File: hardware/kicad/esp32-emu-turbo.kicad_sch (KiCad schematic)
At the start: 53 parts, among them J1 USB_C, J2 PSP_Joystick, SW1 UP, SW10 SELECT, SW11 L, SW12 R, SW2 DOWN, SW3 LEFT, SW4 RIGHT, SW5 A, SW6 B, SW7 X, SW8 Y, SW9 START, U1 ESP32-S3-N16R8, U2 IP5306_USB-C, U3 AMS1117-3.3, U4 ST7796S 4.0in 8080, U5 PAM8403, U6 SD_Card_SPI

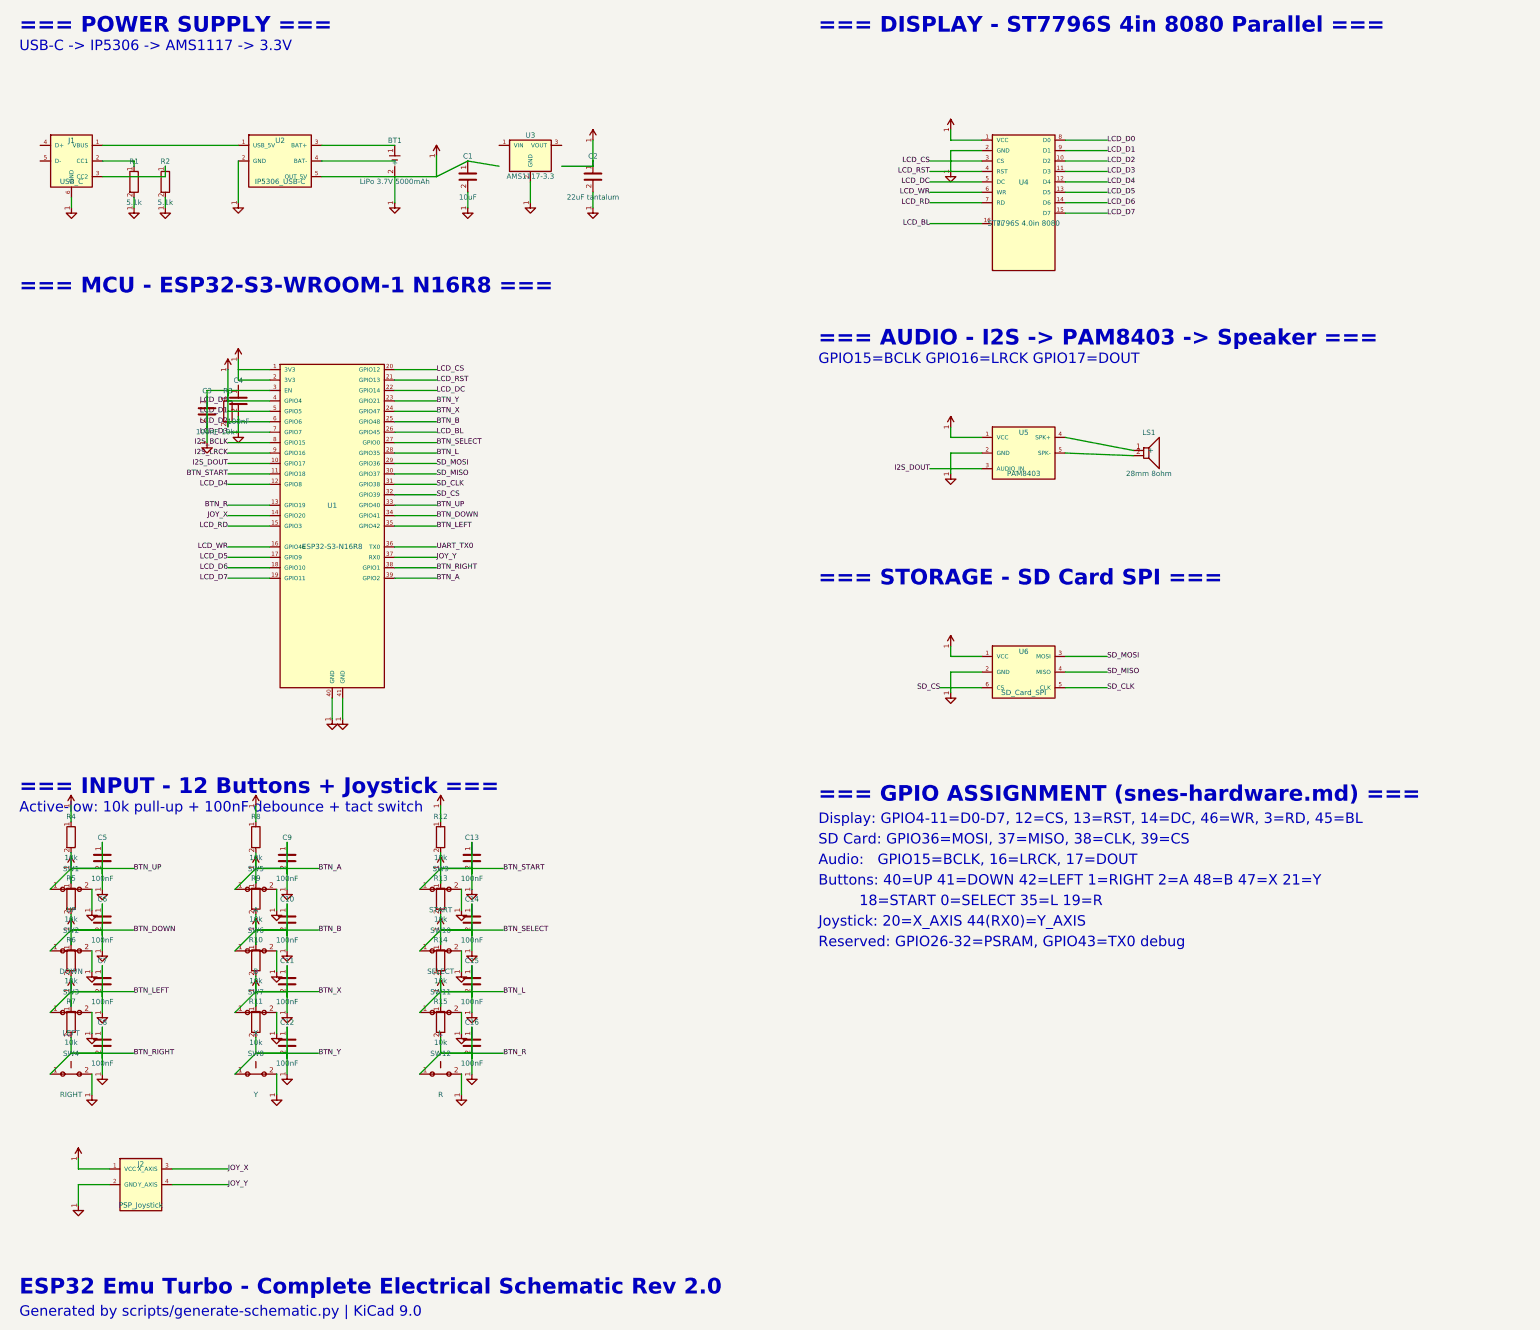
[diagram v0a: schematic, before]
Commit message: Add PCB layout, hierarchical schematics, verification & rendering pipeline
- Reorganize passive components into centered rows below ESP32
- Add missing schematic symbols (LED, FPC_16P, SW_PWR, SW13, SPK1)
- Generate hierarchical root schematic with 7 sub-sheet references
- Create PCB layout generator (4-layer, 160x75mm, JLCPCB-ready)
- Add JLCPCB export (BOM.csv + CPL.csv for 65 components)
- Add schematic/PCB/JLCPCB consistency verification script
- Add PCB SVG renderer + PNG/GIF animation pipeline
- Add interactive 3D PCB viewer (Three.js)
- Update docs (pcb.md, components.md, README.md)

Co-Authored-By: Claude Opus 4.6 <noreply@anthropic.com>
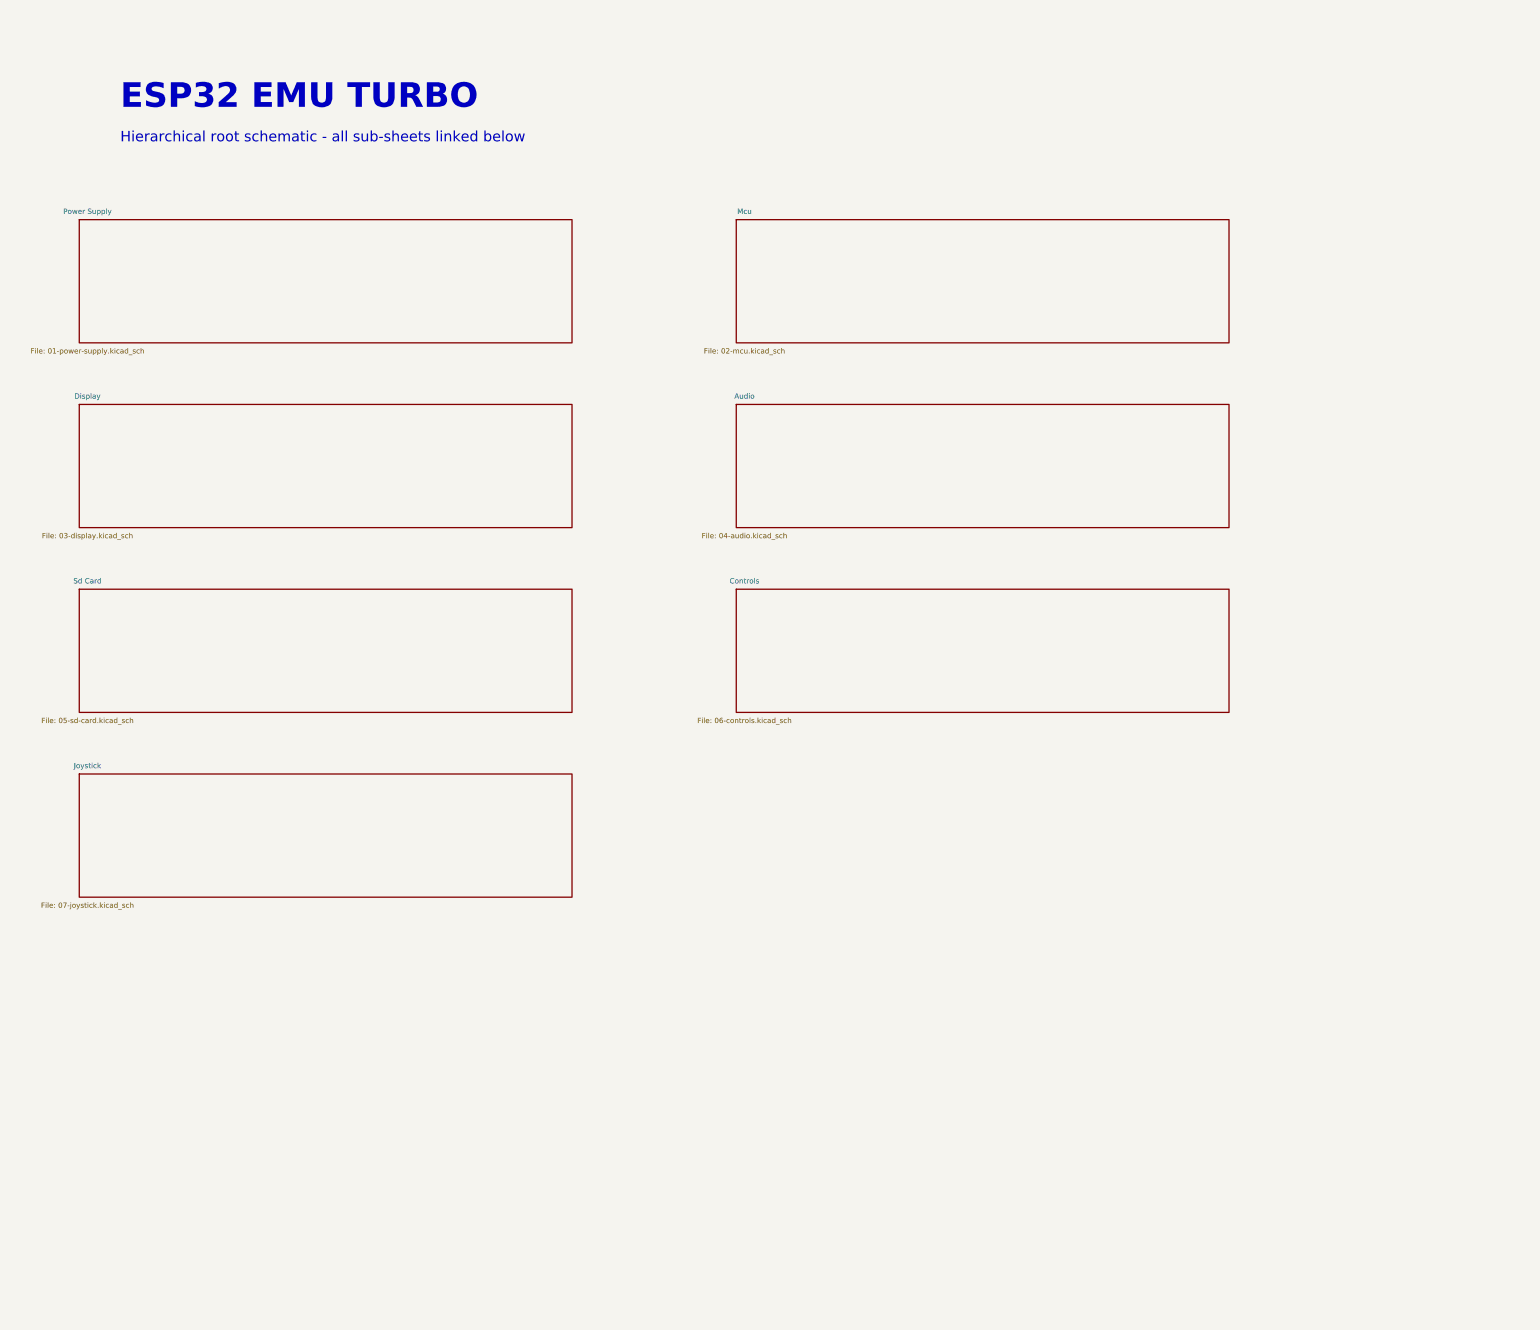
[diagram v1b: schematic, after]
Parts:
- removed BT1: LiPo 3.7V 5000mAh, symbol Battery
- removed C1: 10uF, symbol C
- removed C10, C11, C12, C13, C14, C15, C16, C3, C4, C5, C6, C7, C8, C9: 100nF, symbol C
- removed C2: 22uF tantalum, symbol C
- removed J1: USB_C, symbol USB_C
- removed J2: PSP_Joystick, symbol PSP_Joystick
- removed LS1: 28mm 8ohm, symbol Speaker
- removed R1, R2: 5.1k, symbol R
- removed R10, R11, R12, R13, R14, R15, R3, R4, R5, R6, R7, R8, R9: 10k, symbol R
- removed SW1: UP, symbol SW_Push
- removed SW10: SELECT, symbol SW_Push
- removed SW11: L, symbol SW_Push
- removed SW12: R, symbol SW_Push
- removed SW2: DOWN, symbol SW_Push
- removed SW3: LEFT, symbol SW_Push
- removed SW4: RIGHT, symbol SW_Push
- removed SW5: A, symbol SW_Push
- removed SW6: B, symbol SW_Push
- removed SW7: X, symbol SW_Push
- removed SW8: Y, symbol SW_Push
- removed SW9: START, symbol SW_Push
- removed U1: ESP32-S3-N16R8, symbol ESP32-S3-WROOM-1
- removed U2: IP5306_USB-C, symbol IP5306_Module
- removed U3: AMS1117-3.3, symbol AMS1117-3.3
- removed U4: ST7796S 4.0in 8080, symbol ST7796S_Module
- removed U5: PAM8403, symbol PAM8403_Module
- removed U6: SD_Card_SPI, symbol SD_Module
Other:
- added sheet Audio (04-audio.kicad_sch)
- added sheet Controls (06-controls.kicad_sch)
- added sheet Display (03-display.kicad_sch)
- added sheet Joystick (07-joystick.kicad_sch)
- added sheet Mcu (02-mcu.kicad_sch)
- added sheet Power Supply (01-power-supply.kicad_sch)
- added sheet Sd Card (05-sd-card.kicad_sch)
- note added: "ESP32 EMU TURBO"
- note added: "Hierarchical root schematic - all sub-sheets linked below"
- note removed: "18=START 0=SELECT 35=L 19=R"
- note removed: "=== AUDIO - I2S -> PAM8403 -> Speaker ==="
- note removed: "=== DISPLAY - ST7796S 4in 8080 Parallel ==="
- note removed: "=== GPIO ASSIGNMENT (snes-hardware.md) ==="
- note removed: "=== INPUT - 12 Buttons + Joystick ==="
- note removed: "=== MCU - ESP32-S3-WROOM-1 N16R8 ==="
- note removed: "=== POWER SUPPLY ==="
- note removed: "=== STORAGE - SD Card SPI ==="
- note removed: "Active-low: 10k pull-up + 100nF debounce + tact switch"
- note removed: "Audio: GPIO15=BCLK, 16=LRCK, 17=DOUT"
- note removed: "Buttons: 40=UP 41=DOWN 42=LEFT 1=RIGHT 2=A 48=B 47=X 21=Y"
- note removed: "Display: GPIO4-11=D0-D7, 12=CS, 13=RST, 14=DC, 46=WR, 3=RD, 45=BL"
- note removed: "ESP32 Emu Turbo - Complete Electrical Schematic Rev 2.0"
- note removed: "GPIO15=BCLK GPIO16=LRCK GPIO17=DOUT"
- note removed: "Generated by scripts/generate-schematic.py | KiCad 9.0"
- note removed: "Joystick: 20=X_AXIS 44(RX0)=Y_AXIS"
- note removed: "Reserved: GPIO26-32=PSRAM, GPIO43=TX0 debug"
- note removed: "SD Card: GPIO36=MOSI, 37=MISO, 38=CLK, 39=CS"
- note removed: "USB-C -> IP5306 -> AMS1117 -> 3.3V"
- title: (none) -> ESP32 Emu Turbo - Root Schematic

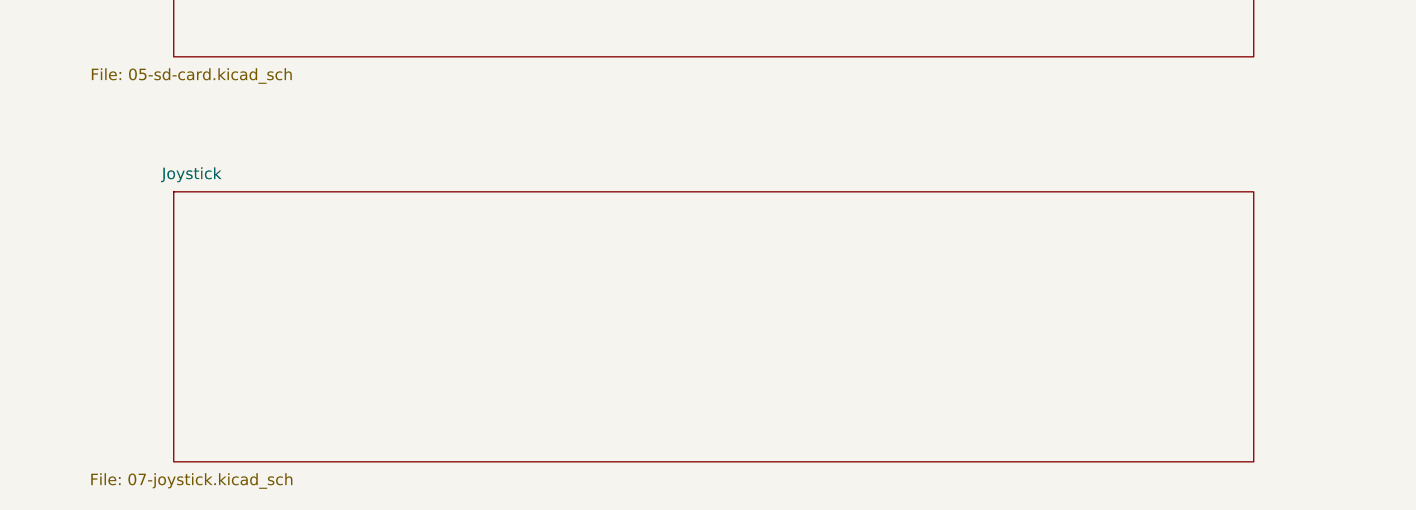
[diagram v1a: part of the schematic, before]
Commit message: Route USB D+/D- to ESP32-S3 GPIO19/20 for native firmware flashing
- Connect USB-C data lines to ESP32-S3 native USB pins (GPIO19=D-, GPIO20=D+)
- Relocate BTN_R from GPIO19 to GPIO43 (TX0, freed by USB replacing UART debug)
- Fix _PIN_TO_GPIO mapping bug: pins 36/37 → GPIO43/44, pins 38/39 → GPIO1/2
- Remove joystick (JOY_X/JOY_Y) — GPIO20 freed for USB, joystick needs both axes
- Increase FPC GND via drill 0.15→0.20mm / pad 0.40→0.45mm (avoid JLCPCB surcharge)
- Add 14 USB regression tests (pin mapping, trace routing, firmware sync, micro-via guard)
- Update all docs, schematics, firmware config, BOM/CPL, gerbers

DFM: 88/88 PASS | DFA: 9/9 PASS

Co-Authored-By: Claude Opus 4.6 <noreply@anthropic.com>
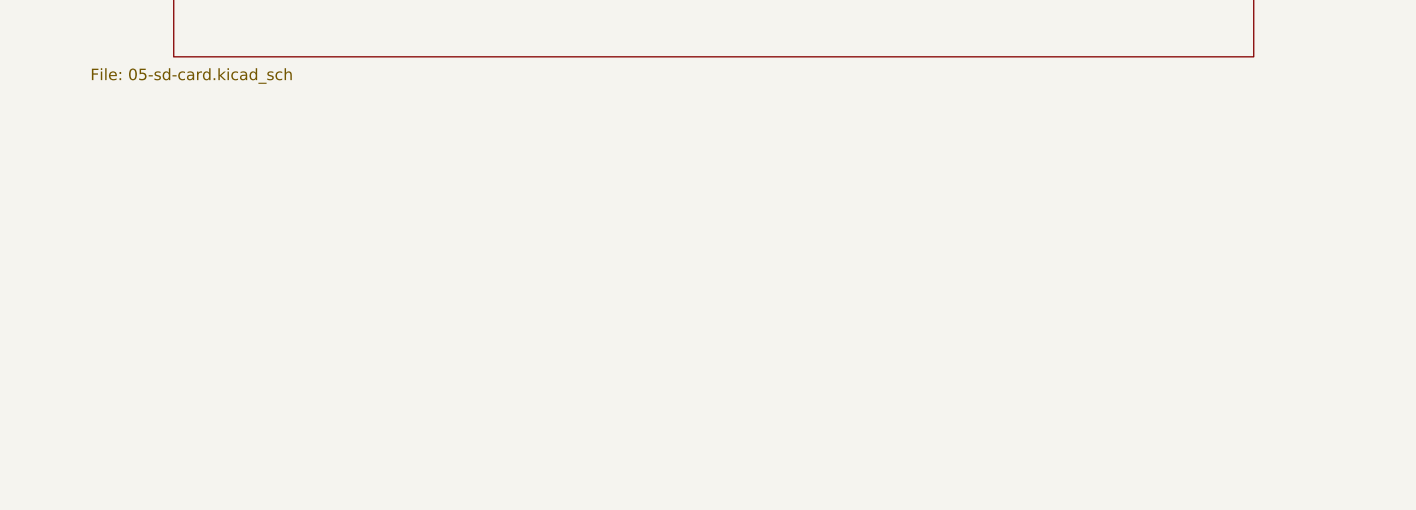
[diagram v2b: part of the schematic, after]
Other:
- removed sheet Joystick
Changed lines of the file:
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@@
-      (effects (font (size 1.27 1.27))))
-  )
-  (sheet (at 40 195) (size 120 30)
-    (stroke (width 0.001) (type solid))
-    (fill (type none))
-    (property "Sheetname" "Joystick"
-      (at 42 193 0)
-      (effects (font (size 1.27 1.27))))
-    (property "Sheetfile" "07-joystick.kicad_sch"
-      (at 42 227 0)
       (effects (font (size 1.27 1.27))))
   )
@@
     (path "/00000006-cafe-4000-8000-000000000006" (page "6"))
     (path "/00000007-cafe-4000-8000-000000000007" (page "7"))
-    (path "/00000008-cafe-4000-8000-000000000008" (page "8"))
   )
 )
